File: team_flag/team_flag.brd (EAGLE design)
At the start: 40.6 x 40.6 mm, 9 parts, among them Q1 MOSFET-NCHANNELSMD, Q2 MOSFET-NCHANNELSMD

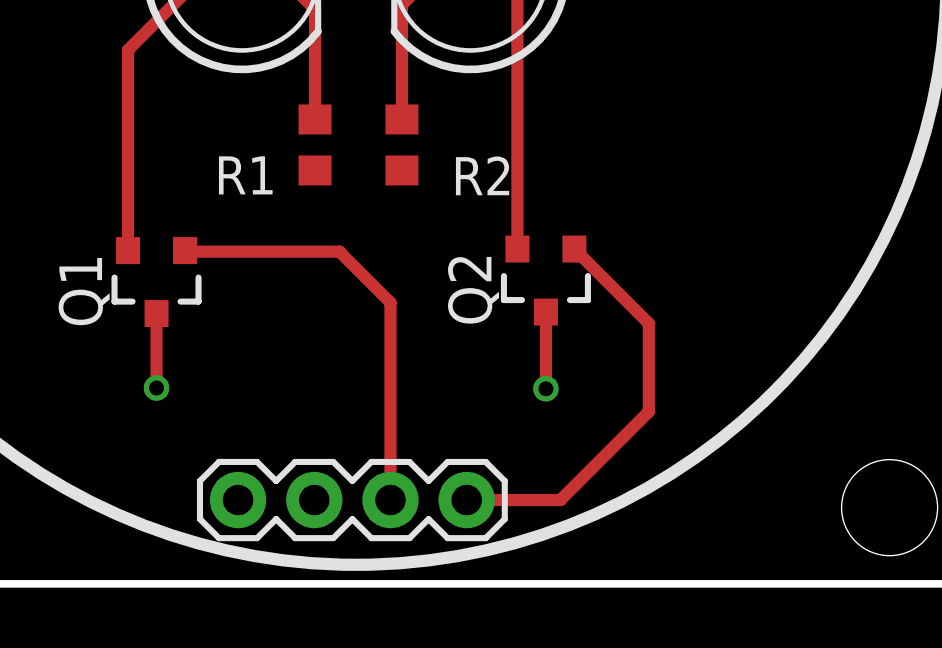
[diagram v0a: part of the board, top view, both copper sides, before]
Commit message: Team Flag pull down resistors
-Added pull down resistors to fix issue with LEDs
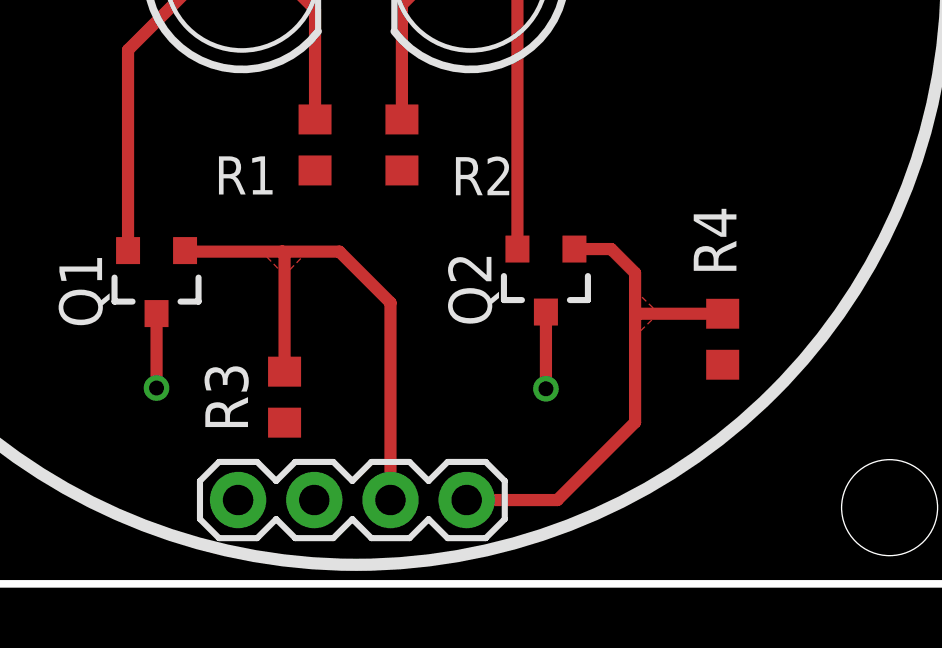
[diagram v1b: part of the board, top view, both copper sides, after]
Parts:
- added R3, R4: 1000, rcl:R0603
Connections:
- net BLUE: now also R3.2
- net GND: now also R3.1, R4.1
- net YELLOW: now also R4.2
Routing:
- net BLUE: track 14.1 -> 18.2 mm
- net YELLOW: track 13.7 -> 17.0 mm
- added copper zone on layer 1, net BLUE
- added copper zone on layer 1, net YELLOW
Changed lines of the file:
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@@
 <layers>
 <layer number="1" name="Top" color="4" fill="1" visible="yes" active="yes"/>
-<layer number="16" name="Bottom" color="1" fill="1" visible="yes" active="yes"/>
+<layer number="16" name="Bottom" color="1" fill="1" visible="no" active="yes"/>
 <layer number="17" name="Pads" color="2" fill="1" visible="yes" active="yes"/>
 <layer number="18" name="Vias" color="2" fill="1" visible="yes" active="yes"/>
@@
 <layer number="20" name="Dimension" color="15" fill="1" visible="yes" active="yes"/>
 <layer number="21" name="tPlace" color="7" fill="1" visible="yes" active="yes"/>
-<layer number="22" name="bPlace" color="14" fill="1" visible="yes" active="yes"/>
+<layer number="22" name="bPlace" color="14" fill="1" visible="no" active="yes"/>
 <layer number="23" name="tOrigins" color="15" fill="1" visible="yes" active="yes"/>
-<layer number="24" name="bOrigins" color="15" fill="1" visible="yes" active="yes"/>
+<layer number="24" name="bOrigins" color="15" fill="1" visible="no" active="yes"/>
 <layer number="25" name="tNames" color="7" fill="1" visible="yes" active="yes"/>
-<layer number="26" name="bNames" color="7" fill="1" visible="yes" active="yes"/>
+<layer number="26" name="bNames" color="7" fill="1" visible="no" active="yes"/>
 <layer number="27" name="tValues" color="7" fill="1" visible="yes" active="yes"/>
-<layer number="28" name="bValues" color="7" fill="1" visible="yes" active="yes"/>
+<layer number="28" name="bValues" color="7" fill="1" visible="no" active="yes"/>
 <layer number="29" name="tStop" color="7" fill="3" visible="yes" active="yes"/>
 <layer number="30" name="bStop" color="7" fill="6" visible="yes" active="yes"/>
@@
 <attribute name="VALUE" x="15.113" y="-0.381" size="1.27" layer="27" font="vector"/>
 </element>
+<element name="R3" library="rcl" package="R0603" value="1000" x="17.9324" y="6.223" smashed="yes" rot="R90">
+<attribute name="NAME" x="16.7132" y="5.0546" size="1.4224" layer="25" font="vector" rot="R90"/>
+<attribute name="VALUE" x="20.5232" y="4.953" size="1.4224" layer="27" font="vector" rot="R90"/>
+</element>
+<element name="R4" library="rcl" package="R0603" value="1000" x="32.5374" y="8.1534" smashed="yes" rot="R90">
+<attribute name="NAME" x="32.9946" y="10.2616" size="1.4224" layer="25" font="vector" rot="R90"/>
+<attribute name="VALUE" x="35.1028" y="8.0518" size="1.4224" layer="27" font="vector" rot="R90"/>
+</element>
 </elements>
 <signals>
 <signal name="YELLOW">
 <contactref element="JP1" pad="4"/>
-<wire x1="24.003" y1="2.794" x2="27.1272" y2="2.794" width="0.4064" layer="1"/>
-<wire x1="27.1272" y1="2.794" x2="30.0736" y2="5.7404" width="0.4064" layer="1"/>
-<wire x1="30.0736" y1="5.7404" x2="30.0736" y2="8.681" width="0.4064" layer="1"/>
 <contactref element="Q2" pad="1"/>
-<wire x1="30.0736" y1="8.681" x2="27.5946" y2="11.16" width="0.4064" layer="1"/>
+<contactref element="R4" pad="2"/>
+<wire x1="27.5946" y1="11.16" x2="28.8196" y2="11.16" width="0.4064" layer="1"/>
+<wire x1="28.8196" y1="11.16" x2="29.6164" y2="10.3632" width="0.4064" layer="1"/>
+<wire x1="29.6164" y1="10.3632" x2="29.6164" y2="9.0932" width="0.4064" layer="1"/>
+<wire x1="29.6164" y1="9.0932" x2="29.6164" y2="5.3848" width="0.4064" layer="1"/>
+<wire x1="29.6164" y1="5.3848" x2="27.0256" y2="2.794" width="0.4064" layer="1"/>
+<wire x1="27.0256" y1="2.794" x2="24.003" y2="2.794" width="0.4064" layer="1"/>
+<wire x1="32.5374" y1="9.0034" x2="29.7062" y2="9.0034" width="0.4064" layer="1"/>
+<wire x1="29.7062" y1="9.0034" x2="29.6164" y2="9.0932" width="0.4064" layer="1"/>
+<polygon width="0.4064" layer="1">
+<vertex x="29.6164" y="8.255"/>
+<vertex x="29.6164" y="9.779"/>
+<vertex x="30.4038" y="9.017"/>
+</polygon>
 </signal>
 <signal name="5V">
@@
 <contactref element="R2" pad="1"/>
 <contactref element="JP1" pad="1"/>
-<polygon width="0.4064" layer="1">
+<polygon width="0.4064" layer="1" rank="2">
 <vertex x="0" y="0"/>
 <vertex x="40.64" y="0"/>
@@
 <vertex x="0" y="40.64"/>
 </polygon>
+<contactref element="R3" pad="1"/>
+<contactref element="R4" pad="1"/>
 </signal>
 <signal name="BLUE">
@@
 <wire x1="21.463" y1="2.794" x2="21.463" y2="9.3726" width="0.4064" layer="1"/>
 <wire x1="21.463" y1="9.3726" x2="19.7612" y2="11.0744" width="0.4064" layer="1"/>
-<wire x1="19.7612" y1="11.0744" x2="14.65" y2="11.0744" width="0.4064" layer="1"/>
+<wire x1="19.7612" y1="11.0744" x2="17.8562" y2="11.0744" width="0.4064" layer="1"/>
+<wire x1="17.8562" y1="11.0744" x2="14.65" y2="11.0744" width="0.4064" layer="1"/>
 <wire x1="14.65" y1="11.0744" x2="14.6152" y2="11.1092" width="0.4064" layer="1"/>
+<contactref element="R3" pad="2"/>
+<wire x1="17.9324" y1="7.073" x2="17.9324" y2="10.9982" width="0.4064" layer="1"/>
+<wire x1="17.9324" y1="10.9982" x2="17.8562" y2="11.0744" width="0.4064" layer="1"/>
+<polygon width="0.4064" layer="1">
+<vertex x="17.1704" y="11.0744"/>
+<vertex x="18.6944" y="11.0744"/>
+<vertex x="17.9324" y="10.287"/>
+</polygon>
 </signal>
 </signals>

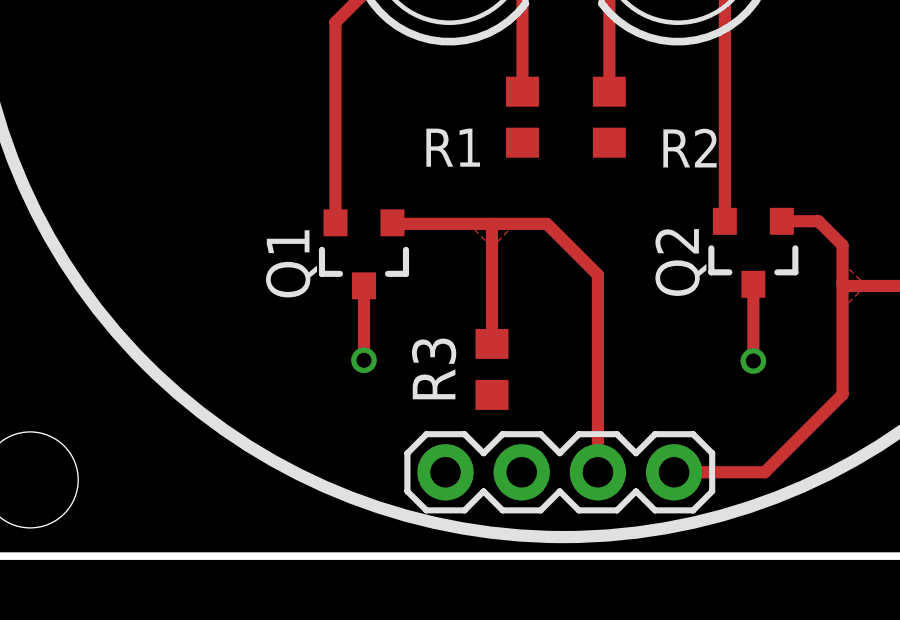
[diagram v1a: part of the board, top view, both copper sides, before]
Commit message: Team Flag new mosfets
-replaced old mosfets with logic-level mosfets
-changed pull down resistor value to 10K
-renamed 5V signal to VCC
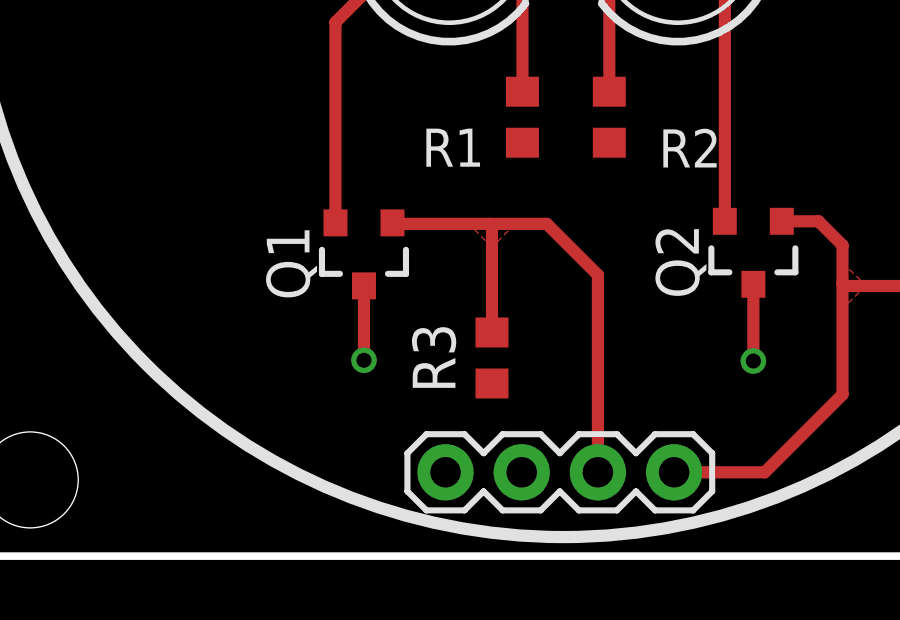
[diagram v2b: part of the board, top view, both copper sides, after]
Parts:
- Q1, Q2: value MOSFET-NCHANNELSMD -> MOSFET-LOGIC-NCHANNELSMD; device pie:SOT23-3 -> pie:SOT23-3-LOGIC
- R3, R4: value 1000 -> 10K
- moved R3 0.38 mm to (17.9, 6.60)
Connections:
- net 5V renamed VCC
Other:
- board text added: "VCC"
- board text removed: "5V"
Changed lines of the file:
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@@
 <layers>
 <layer number="1" name="Top" color="4" fill="1" visible="yes" active="yes"/>
-<layer number="16" name="Bottom" color="1" fill="1" visible="no" active="yes"/>
+<layer number="16" name="Bottom" color="1" fill="1" visible="yes" active="yes"/>
 <layer number="17" name="Pads" color="2" fill="1" visible="yes" active="yes"/>
 <layer number="18" name="Vias" color="2" fill="1" visible="yes" active="yes"/>
@@
 <layer number="20" name="Dimension" color="15" fill="1" visible="yes" active="yes"/>
 <layer number="21" name="tPlace" color="7" fill="1" visible="yes" active="yes"/>
-<layer number="22" name="bPlace" color="14" fill="1" visible="no" active="yes"/>
+<layer number="22" name="bPlace" color="14" fill="1" visible="yes" active="yes"/>
 <layer number="23" name="tOrigins" color="15" fill="1" visible="yes" active="yes"/>
-<layer number="24" name="bOrigins" color="15" fill="1" visible="no" active="yes"/>
+<layer number="24" name="bOrigins" color="15" fill="1" visible="yes" active="yes"/>
 <layer number="25" name="tNames" color="7" fill="1" visible="yes" active="yes"/>
-<layer number="26" name="bNames" color="7" fill="1" visible="no" active="yes"/>
+<layer number="26" name="bNames" color="7" fill="1" visible="yes" active="yes"/>
 <layer number="27" name="tValues" color="7" fill="1" visible="yes" active="yes"/>
-<layer number="28" name="bValues" color="7" fill="1" visible="no" active="yes"/>
+<layer number="28" name="bValues" color="7" fill="1" visible="yes" active="yes"/>
 <layer number="29" name="tStop" color="7" fill="3" visible="yes" active="yes"/>
 <layer number="30" name="bStop" color="7" fill="6" visible="yes" active="yes"/>
@@
 This design is open source hardware.
 pioneers.berkeley.edu/opensource</text>
-<text x="18.034" y="4.572" size="1.4224" layer="28" font="vector" rot="MR270" align="top-right">5V</text>
+<text x="18.034" y="4.572" size="1.4224" layer="28" font="vector" rot="MR270" align="top-right">VCC</text>
 <text x="10.2108" y="35.052" size="1.4224" layer="22" font="vector" ratio="15" rot="MR0" align="top-right">Version 2.0, Rev B</text>
 </plain>
@@
 <element name="U$2" library="pie" package="OSHW-LOGO-S" value="" x="20.32" y="31.75" rot="MR0"/>
 <element name="U$1" library="pie" package="PIE-LOGO-SMALL" value="" x="33.655" y="16.51" rot="MR0"/>
-<element name="Q1" library="pie" package="SOT23-3" value="MOSFET-NCHANNELSMD" x="13.6652" y="10.1092" smashed="yes" rot="R180">
+<element name="Q1" library="pie" package="SOT23-3-LOGIC" value="MOSFET-LOGIC-NCHANNELSMD" x="13.6652" y="10.1092" smashed="yes" rot="R180">
 <attribute name="NAME" x="10.4267" y="11.0236" size="1.4224" layer="25" font="vector" rot="R90" align="top-right"/>
-</element>
-<element name="Q2" library="pie" package="SOT23-3" value="MOSFET-NCHANNELSMD" x="26.6446" y="10.16" smashed="yes" rot="R180">
+<attribute name="PIE_DIGIKEY-PN" value="DMN65D8L-7DICT-ND" x="13.6652" y="10.1092" size="1.778" layer="27" rot="R180" display="off"/>
+</element>
+<element name="Q2" library="pie" package="SOT23-3-LOGIC" value="MOSFET-LOGIC-NCHANNELSMD" x="26.6446" y="10.16" smashed="yes" rot="R180">
 <attribute name="NAME" x="23.4061" y="11.0744" size="1.4224" layer="25" font="vector" rot="R270"/>
+<attribute name="PIE_DIGIKEY-PN" value="DMN65D8L-7DICT-ND" x="26.6446" y="10.16" size="1.778" layer="27" rot="R180" display="off"/>
 </element>
 <element name="JP1" library="pie" package="1X04" value="" x="20.193" y="2.794" smashed="yes">
 <attribute name="VALUE" x="15.113" y="-0.381" size="1.27" layer="27" font="vector"/>
 </element>
-<element name="R3" library="rcl" package="R0603" value="1000" x="17.9324" y="6.223" smashed="yes" rot="R90">
-<attribute name="NAME" x="16.7132" y="5.0546" size="1.4224" layer="25" font="vector" rot="R90"/>
-<attribute name="VALUE" x="20.5232" y="4.953" size="1.4224" layer="27" font="vector" rot="R90"/>
-</element>
-<element name="R4" library="rcl" package="R0603" value="1000" x="32.5374" y="8.1534" smashed="yes" rot="R90">
+<element name="R3" library="rcl" package="R0603" value="10K" x="17.9324" y="6.604" smashed="yes" rot="R90">
+<attribute name="NAME" x="16.7132" y="5.4356" size="1.4224" layer="25" font="vector" rot="R90"/>
+<attribute name="VALUE" x="20.5232" y="5.334" size="1.4224" layer="27" font="vector" rot="R90"/>
+</element>
+<element name="R4" library="rcl" package="R0603" value="10K" x="32.5374" y="8.1534" smashed="yes" rot="R90">
 <attribute name="NAME" x="32.9946" y="10.2616" size="1.4224" layer="25" font="vector" rot="R90"/>
-<attribute name="VALUE" x="35.1028" y="8.0518" size="1.4224" layer="27" font="vector" rot="R90"/>
+<attribute name="VALUE" x="35.1536" y="8.9662" size="1.4224" layer="27" font="vector" rot="R90"/>
 </element>
 </elements>
@@
 </polygon>
 </signal>
-<signal name="5V">
+<signal name="VCC">
 <contactref element="JP1" pad="2"/>
 <polygon width="0.4064" layer="16">
@@
 <wire x1="14.65" y1="11.0744" x2="14.6152" y2="11.1092" width="0.4064" layer="1"/>
 <contactref element="R3" pad="2"/>
-<wire x1="17.9324" y1="7.073" x2="17.9324" y2="10.9982" width="0.4064" layer="1"/>
+<wire x1="17.9324" y1="7.454" x2="17.9324" y2="10.9982" width="0.4064" layer="1"/>
 <wire x1="17.9324" y1="10.9982" x2="17.8562" y2="11.0744" width="0.4064" layer="1"/>
 <polygon width="0.4064" layer="1">

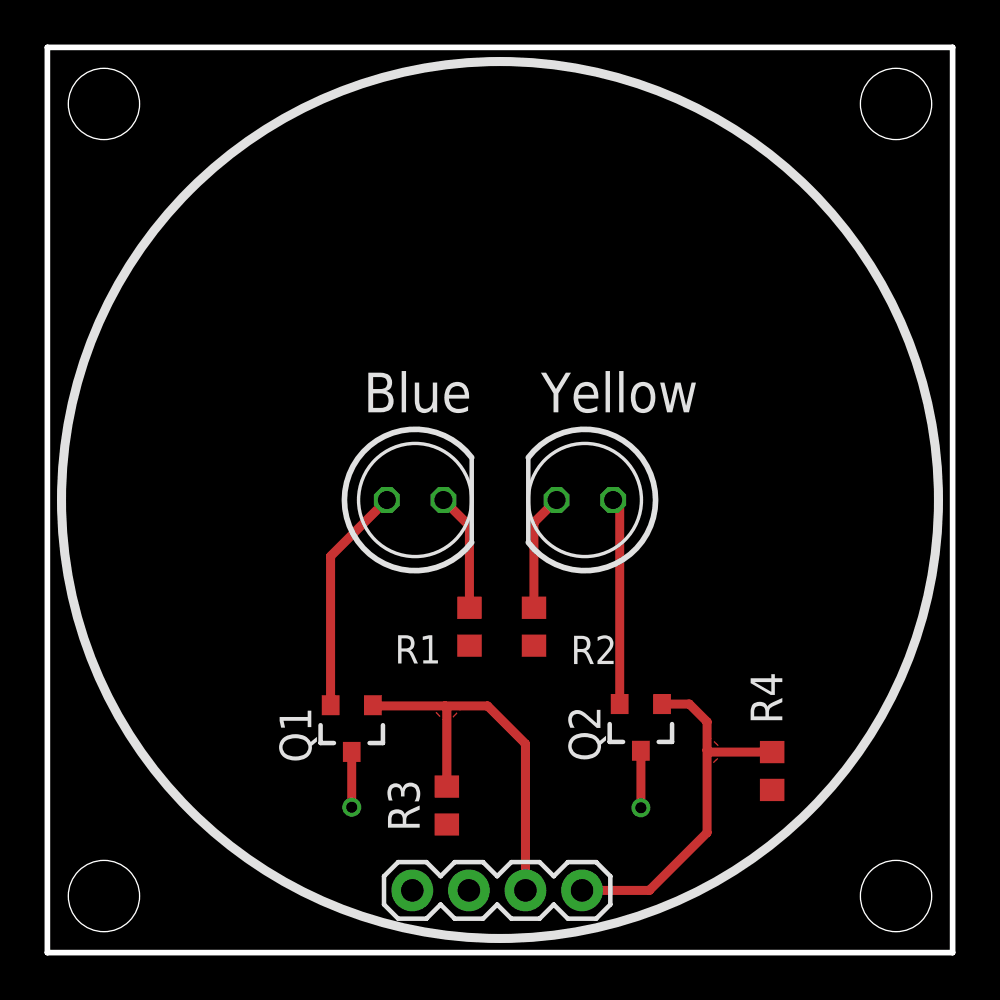
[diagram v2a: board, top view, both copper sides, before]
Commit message: Team Flag Rev C
-rearranged circuitry
-Used proper 4-pin MTA footprint
-Moved bPlace signal labels to be more visible
-Replaced 330 Ohm with 200 Ohm resistors
-Updated silkscreen and schematic information
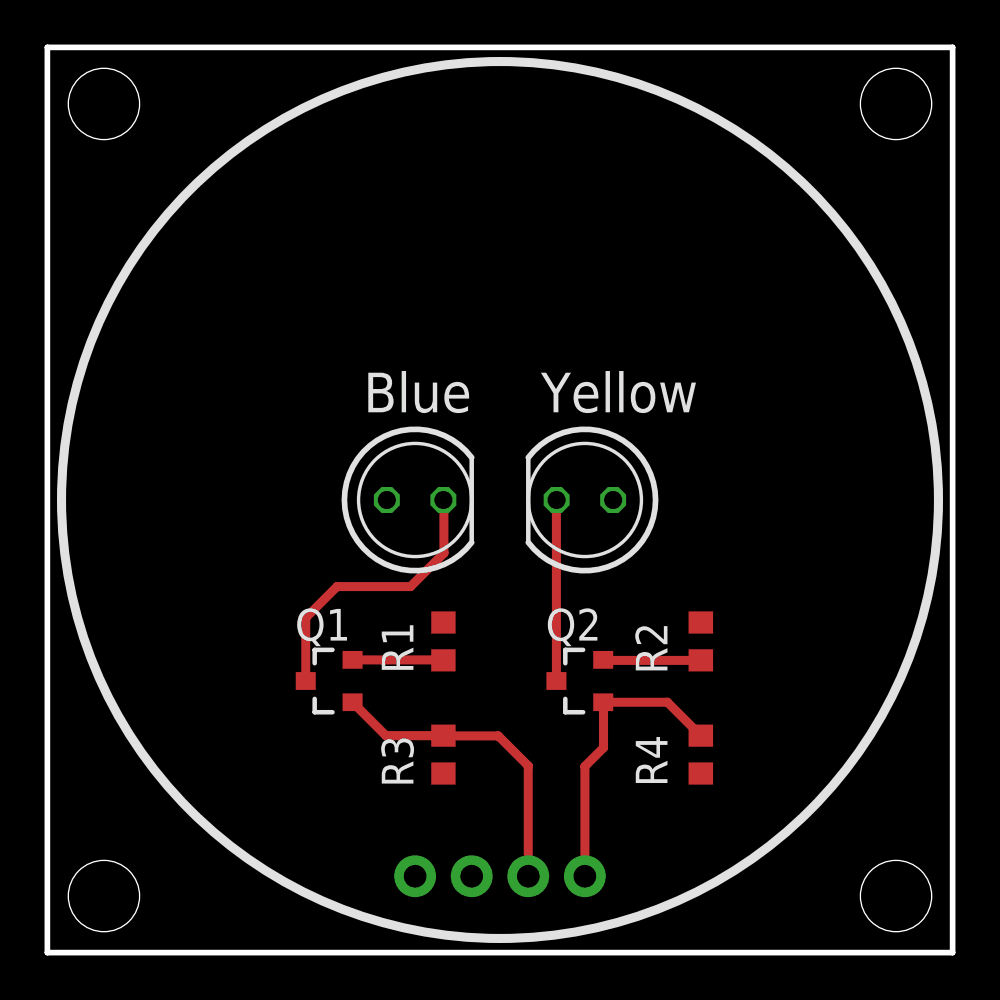
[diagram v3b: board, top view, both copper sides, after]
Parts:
- JP1: device pie:1X04 -> pie:1X04-MTA
- R1, R2: value 330 -> 200
- moved R2 7.52 mm to (29.3, 14.0), turned to 270 degrees
- moved Q2 3.37 mm to (24.0, 12.2), turned to 90 degrees
- moved R4 3.28 mm to (29.3, 8.89)
- moved Q1 2.30 mm to (12.7, 12.2), turned to 90 degrees
- moved R3 2.29 mm to (17.8, 8.89)
- moved R1 1.34 mm to (17.8, 14.0), turned to 270 degrees
- moved JP1 0.65 mm to (20.3, 3.43), flipped to the bottom, turned to 180 degrees
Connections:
- removed net BSIGNAL: LED1.A, Q1.2
- removed net YSIGNAL: LED2.A, Q2.2
- new net BSOURCE: Q1.2, R1.2
- new net YSOURCE: Q2.2, R2.2
- net BDRAIN: now also Q1.3; no longer R1.2
- net VCC: now also LED1.A, LED2.A; no longer Q1.3, Q2.3
- net YDRAIN: now also Q2.3; no longer R2.2
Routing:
- net BSIGNAL: track 10.3 -> 0.00 mm
- net YSIGNAL: track 9.28 -> 0.00 mm
- net BDRAIN: track 5.32 -> 12.6 mm
- net VCC: track 5.04 -> 0.00 mm, vias 2 -> 0
- net YSOURCE: track 0.00 -> 4.41 mm
- net BSOURCE: track 0.00 -> 4.10 mm
- net YELLOW: track 17.0 -> 13.2 mm
- net BLUE: track 17.8 -> 14.0 mm
- net YDRAIN: track 5.26 -> 8.13 mm
- removed copper zone on layer 1, net BLUE
- removed copper zone on layer 1, net YELLOW
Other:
- board text added: "Pioneers in Engineering Team Flag 1/1/14 Version 2.0, Rev C"
- board text removed: "Pioneers in Engineering"
- board text removed: "Team Flag 11/13/13"
- board text removed: "Version 2.0, Rev B"
